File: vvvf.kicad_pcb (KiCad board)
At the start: 4 copper layers, 100 x 100 mm, 75 parts, among them Q3 IPDD60R037CM8XTMA1, Q4 IPDD60R037CM8XTMA1, Q5 IPDD60R037CM8XTMA1, Q6 IPDD60R037CM8XTMA1, Q7 IPDD60R037CM8XTMA1, Q8 IPDD60R037CM8XTMA1, Q9 IPDD60R037CM8XTMA1, U3 UCC21520ADW, U5 ACS770xCB-200B-PFF, U6 UCC21520ADW, U7 UCC21520ADW

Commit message: Continue on layout
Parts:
- C10, R11, R12, R14, R24, R25, R26, R27, R9: moved to B.Cu
- D12: moved to F.Cu
- moved R4 126.8 mm to (173.2, 76.8), turned to 90 degrees
- moved R9 115.4 mm to (180.2, 130.5), turned to -90 degrees
- moved C17 90.5 mm to (117.8, 76.8), turned to 90 degrees
- moved C18 90.2 mm to (113.5, 76.7), turned to 90 degrees
- moved C9 89.4 mm to (111.5, 76.8), turned to 90 degrees
- moved C19 79.3 mm to (112.9, 92.2), turned to 180 degrees
- moved R22 75.6 mm to (115.2, 76.7), turned to 90 degrees
- moved C22 71.5 mm to (119.2, 92.2), turned to 180 degrees
- moved C21 68.1 mm to (119.2, 94.8), turned to 180 degrees
- moved C20 65.0 mm to (119.2, 97.3), turned to 180 degrees
- moved R23 64.5 mm to (123.5, 100.2), turned to -90 degrees
- moved C23 61.3 mm to (239.0, 142.0)
- moved R24 60.8 mm to (123.5, 108.5), turned to -90 degrees
- moved R26 56.6 mm to (120.0, 115.8), turned to -90 degrees
- moved R25 50.9 mm to (123.5, 130.8), turned to -90 degrees
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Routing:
- net Net-(J2-Pin_1): track 0.00 -> 25.2 mm
- added copper zone on In2.Cu, net GND

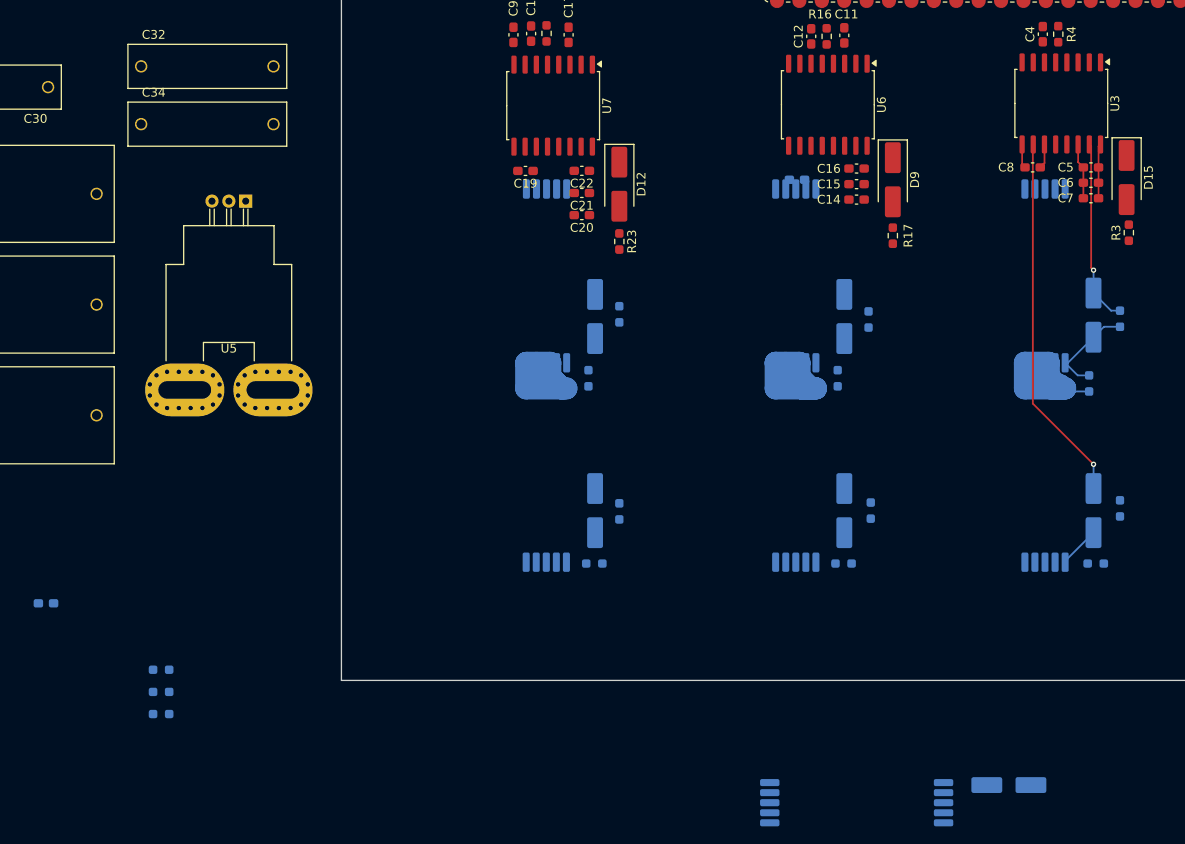
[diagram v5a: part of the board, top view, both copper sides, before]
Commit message: Checkpoint before switching to an external IGBT array
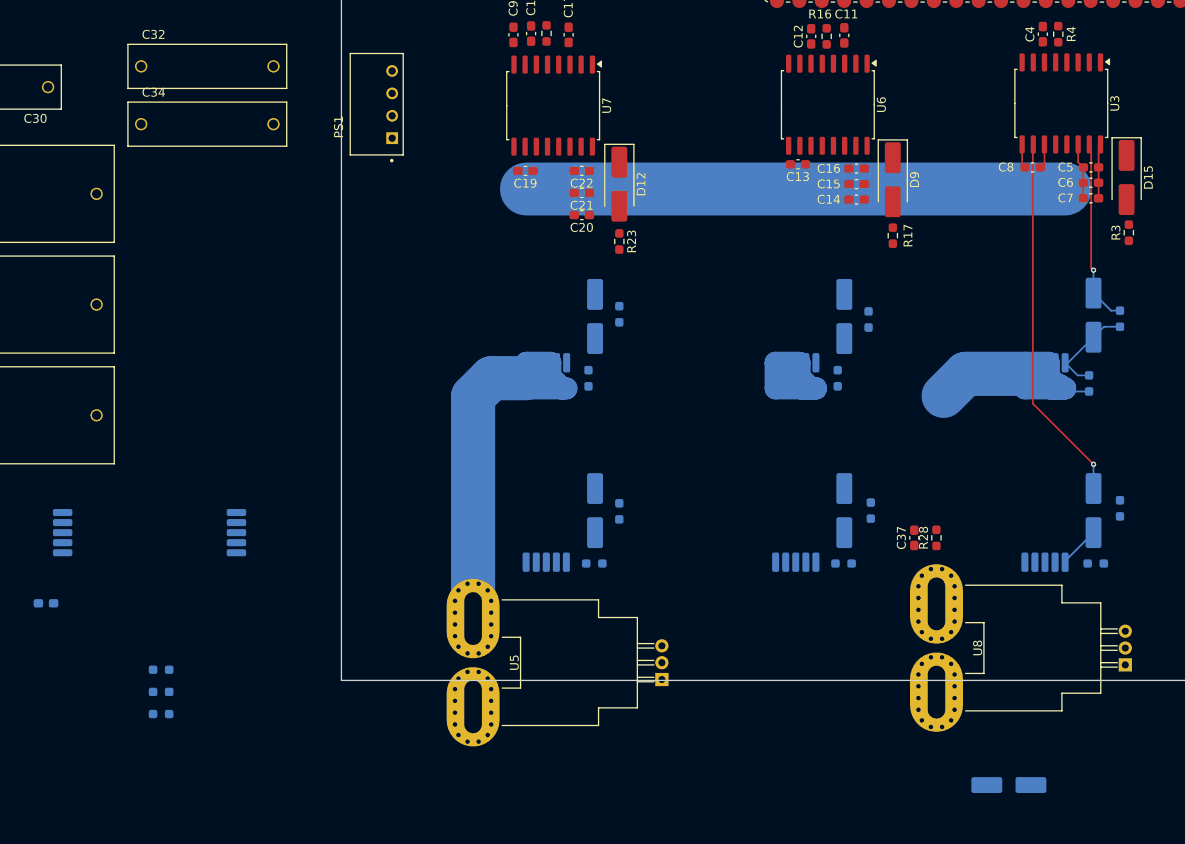
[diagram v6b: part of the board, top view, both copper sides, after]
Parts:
- added C37: 100nF, Capacitor_SMD:C_0603_1608Metric_Pad1.08x0.95mm_HandSolder, F.Cu at (156.9, 133.8)
- added PS1: ROE-1205S, Snapeda:ROE-1205S_CONV_ROE-1205S, F.Cu at (96.0, 84.7)
- added R28: 10k, Resistor_SMD:R_0603_1608Metric_Pad0.98x0.95mm_HandSolder, F.Cu at (159.4, 133.8)
- added U8: ACS770xCB-200B-PFF, Sensor_Current:Allegro_CB_PFF, F.Cu at (180.8, 148.2)
- C13: moved to F.Cu
- moved Q4 85.8 mm to (70.2, 133.2)
- moved U5 71.9 mm to (128.3, 149.9), turned to 90 degrees
- moved C13 1.75 mm to (143.8, 91.5)
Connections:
- net +24V renamed +12V
- A1 pad 36: unconnected-(A1-3V3-Pad36) -> +3V3
- C23 pad 2: Net-(J1-Pin_1) (its old number) -> /C3
- C24 pad 2: Net-(J1-Pin_1) (its old number) -> /C3
- C25 pad 1: Net-(J1-Pin_1) (its old number) -> /C3
- C26 pad 1: Net-(J1-Pin_1) (its old number) -> /C3
- C5 pad 2: Net-(J1-Pin_1) (its old number) -> /C3
- C6 pad 2: Net-(J1-Pin_1) (its old number) -> /C3
- C7 pad 2: Net-(J1-Pin_1) (its old number) -> /C3
- D7 pad 2: +3V3 -> +5V
- Q3 pad 10: Net-(J1-Pin_1) (its old number) -> /C3
- Q3 pad 6: Net-(J1-Pin_1) (its old number) -> /C3
- Q3 pad 7: Net-(J1-Pin_1) (its old number) -> /C3
- Q3 pad 8: Net-(J1-Pin_1) (its old number) -> /C3
- Q3 pad 9: Net-(J1-Pin_1) (its old number) -> /C3
- Q5 pad 2: Net-(J1-Pin_1) (its old number) -> /C3
- Q5 pad 3: Net-(J1-Pin_1) (its old number) -> /C3
- Q5 pad 4: Net-(J1-Pin_1) (its old number) -> /C3
- Q5 pad 5: Net-(J1-Pin_1) (its old number) -> /C3
- R5 pad 2: Net-(J1-Pin_1) (its old number) -> /C3
- U3 pad 14: Net-(J1-Pin_1) (its old number) -> /C3
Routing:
- net Vdrive: track 0.00 -> 61.1 mm
- net /C3: track 0.00 -> 45.2 mm
- net /C1: track 21.3 -> 56.2 mm
- net Net-(J1-Pin_1) (its old number): track 33.9 -> 0.00 mm

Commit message: Starting new routing with external IGBT
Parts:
- removed C10: 100nF, Capacitor_SMD:C_0603_1608Metric_Pad1.08x0.95mm_HandSolder
- removed C23, C25, C27, C29, C31, C33: 1uF, Snapeda:B32923C3105M000_CAPRR2250W80L2650T1100H2050
- removed C24, C26, C28, C30, C32, C34: 100nF, Snapeda:B32922C3104K289_CAPRR1500W80L1800T500H1050
- removed Q3, Q4, Q5, Q6, Q7, Q8, Q9: IPDD60R037CM8XTMA1, Package_TO_SOT_SMD:Infineon_PG-HDSOP-10-1
- removed R14: 10k, Resistor_SMD:R_0603_1608Metric_Pad0.98x0.95mm_HandSolder
- removed U5: ACS770xCB-200B-PFF, Sensor_Current:Allegro_CB_PFF
- added C38: 100nF, Capacitor_SMD:C_0603_1608Metric_Pad1.08x0.95mm_HandSolder, F.Cu at (65.6, 93.2)
- added J1: Conn_01x16_Pin, Connector_PinHeader_2.54mm:PinHeader_1x16_P2.54mm_Vertical, F.Cu at (150.9, 120.6)
- added J2: Screw_Terminal_01x01, easyeda2kicad:CONN-TH_T44001, F.Cu at (35.0, 134.3)
- added J3: Screw_Terminal_01x01, easyeda2kicad:CONN-TH_T44001, F.Cu at (44.3, 134.3)
- added J6: Screw_Terminal_01x02, easyeda2kicad:CONN-TH_WJ126V-5.0-2P, F.Cu at (97.5, 97.0)
- added J7: Screw_Terminal_01x01, easyeda2kicad:CONN-TH_T44001, F.Cu at (69.8, 130.5)
- added J8: Screw_Terminal_01x01, easyeda2kicad:CONN-TH_T44001, F.Cu at (59.8, 131.0)
- added R30: 10k, Resistor_SMD:R_0603_1608Metric_Pad0.98x0.95mm_HandSolder, F.Cu at (65.6, 95.8)
- added U4: TLP152, Package_SO:SO-5-6_4.55x3.7mm_P1.27mm, F.Cu at (61.8, 156.5)
- added U9: ACS758KCB-150B-PFF-T, easyeda2kicad:SENSOR-TH_ACS758KCB-150B-PFF-T, F.Cu at (40.0, 112.6)
- D10, D11, D13, D3, D5, D6, D8, R10, R11, R12, R18, R19, R20, R21, R24, R25, R26, R27, R5, R6, R9: moved to F.Cu
- U8: value ACS770xCB-200B-PFF -> ACS758KCB-150B-PFF-T; footprint Sensor_Current:Allegro_CB_PFF -> easyeda2kicad:SENSOR-TH_ACS758KCB-150B-PFF-T
- moved C37 124.0 mm to (40.0, 92.6)
- moved R28 124.0 mm to (42.5, 92.6)
- moved U8 122.8 mm to (64.2, 109.6), turned to 180 degrees
- moved D6 94.1 mm to (74.0, 153.0), turned to 0 degrees
- moved R25 37.1 mm to (144.3, 100.2)
- moved D13 36.9 mm to (141.5, 100.3)
- moved R27 33.4 mm to (141.3, 110.5), turned to -90 degrees
- moved D5 32.9 mm to (159.0, 99.4)
- moved R19 32.8 mm to (161.7, 99.4)
- moved R23 32.8 mm to (154.8, 90.7)
- moved D3 32.2 mm to (176.9, 98.5)
- moved R9 32.0 mm to (179.7, 98.5)
- moved R21 30.4 mm to (160.1, 108.5)
- moved R26 29.6 mm to (149.3, 111.4), turned to 90 degrees
- moved C18 29.3 mm to (142.8, 78.0)
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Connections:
- net /C1 renamed /IGBT_W_H_E
- net Net-(D10-A) renamed /IGBT_V_H_G
- net Net-(D11-A) renamed /IGBT_W_H_G
- net Net-(D13-A) renamed /IGBT_W_L_G
- net Net-(D3-A) renamed /IGBT_U_L_G
- net Net-(D5-A) renamed /IGBT_V_L_G
- net Net-(D6-A) renamed /IGBT_BRAKE_G
- net Net-(D8-A) renamed /IGBT_U_H_G
- net Net-(J1-Pin_1) renamed /IGBT_V_H_E
- C5 pad 2: /C3 -> /IGBT_U_H_E
- C6 pad 2: /C3 -> /IGBT_U_H_E
- C7 pad 2: /C3 -> /IGBT_U_H_E
- R28 pad 1: Net-(U8-VIOUT) -> Net-(U9-VOUT)
- R28 pad 2: /GP26 -> /ADC1
- R5 pad 2: /C3 -> /IGBT_U_H_E
- U3 pad 14: /C3 -> /IGBT_U_H_E
- U8 pad 3: Net-(U8-VIOUT) -> Net-(U8-VOUT)
- U8 pad 4: /C3 -> Net-(J8-Pin_1)
- U8 pad 5: /C4 -> Net-(J7-Pin_1)
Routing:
- net Vdrive: track 61.1 -> 0.00 mm
- net /IGBT_W_H_E: track 56.2 -> 6.49 mm
- net /C3: track 45.2 -> 0.00 mm
- net Net-(D3-K): track 41.9 -> 9.87 mm, vias 1 -> 0
- net /IGBT_V_H_E: track 25.2 -> 6.30 mm
- net GND: track 0.00 -> 16.5 mm, vias 0 -> 2
- net +5V: track 0.00 -> 15.7 mm
- net Net-(D11-K): track 0.00 -> 13.3 mm
- net Net-(D10-K): track 0.00 -> 13.1 mm
- net Net-(D13-K): track 0.00 -> 10.8 mm
- net Net-(D5-K): track 0.00 -> 10.3 mm
- net Net-(D9-K): track 0.00 -> 9.69 mm
- net Net-(D12-K): track 0.00 -> 9.63 mm
- net /IGBT_U_H_G: track 11.2 -> 3.41 mm
- net Net-(D8-K): track 20.9 -> 13.3 mm, vias 1 -> 0
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
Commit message: sus commit
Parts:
- added C10: 100nF, Capacitor_SMD:C_0603_1608Metric_Pad1.08x0.95mm_HandSolder, F.Cu at (43.4, 78.9)
- added J4: Screw_Terminal_01x01, easyeda2kicad:CONN-TH_T44001, F.Cu at (77.8, 74.7)
- added J5: Screw_Terminal_01x01, easyeda2kicad:CONN-TH_T44001, F.Cu at (77.8, 84.0)
- added J9: Screw_Terminal_01x02, easyeda2kicad:CONN-TH_WJ126V-5.0-2P, F.Cu at (97.6, 107.9)
- added R13: 10k, Resistor_SMD:R_0603_1608Metric_Pad0.98x0.95mm_HandSolder, F.Cu at (40.9, 78.9)
- added R14: 6.8k, Resistor_SMD:R_0603_1608Metric_Pad0.98x0.95mm_HandSolder, F.Cu at (44.3, 76.3)
- added R15: 1M, Resistor_SMD:R_1206_3216Metric_Pad1.30x1.75mm_HandSolder, F.Cu at (110.8, 102.4)
- added R29: 6.8k, Resistor_SMD:R_0603_1608Metric_Pad0.98x0.95mm_HandSolder, F.Cu at (50.3, 109.2)
- added R31: 6.8k, Resistor_SMD:R_0603_1608Metric_Pad0.98x0.95mm_HandSolder, F.Cu at (27.5, 109.4)
- added R32: 1k, Resistor_SMD:R_1206_3216Metric_Pad1.30x1.75mm_HandSolder, F.Cu at (120.8, 102.4)
- added R33: 1M, Resistor_SMD:R_1206_3216Metric_Pad1.30x1.75mm_HandSolder, F.Cu at (115.8, 102.4)
- added U11: LM7805_TO220, Package_TO_SOT_THT:TO-220-3_Vertical, F.Cu at (110.4, 96.0)
- added U12: AMC1303M2510DWVR, easyeda2kicad:SOIC-8_L7.5-W5.9-P1.27-LS11.5-BL-1, F.Cu at (121.8, 86.0)
- added U5: ACS758KCB-150B-PFF-T, easyeda2kicad:SENSOR-TH_ACS758KCB-150B-PFF-T, F.Cu at (58.8, 79.6)
- moved R12 121.5 mm to (182.0, 111.4), turned to 180 degrees
- moved R11 110.9 mm to (176.6, 124.2)
- moved D6 107.5 mm to (176.8, 121.4)
- moved U4 100.8 mm to (133.4, 85.6), turned to -90 degrees
- moved J7 43.2 mm to (27.9, 141.5)
- moved C38 43.2 mm to (24.4, 106.2)
- moved U8 43.2 mm to (23.0, 122.5)
- moved R30 43.2 mm to (24.4, 108.7)
- moved J8 43.1 mm to (17.9, 141.5)
- moved R27 38.4 mm to (179.2, 116.6), turned to 0 degrees
- moved J2 24.9 mm to (59.0, 140.6), turned to 180 degrees
- moved R5 23.0 mm to (161.5, 116.6), turned to 0 degrees
- moved C37 19.8 mm to (53.6, 107.0)
- moved R28 19.8 mm to (56.1, 107.0)
- moved U9 17.3 mm to (54.6, 121.9)
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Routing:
- net +5V: track 15.7 -> 155.0 mm, vias 0 -> 1
- net +12V: track 6.99 -> 141.5 mm, vias 0 -> 1
- net Net-(D6-K): track 0.00 -> 68.8 mm
- net /IGBT_W_L_G: track 3.44 -> 46.9 mm, vias 0 -> 1
- net /IGBT_U_H_E: track 6.35 -> 37.4 mm, vias 0 -> 1
- net /IGBT_U_H_G: track 3.41 -> 33.2 mm
- net GNDPWR: track 8.86 -> 37.5 mm, vias 2 -> 4
- net /IGBT_V_H_E: track 6.30 -> 33.3 mm
- net /IGBT_V_H_G: track 3.18 -> 27.2 mm, vias 0 -> 2
- net /IGBT_V_L_G: track 3.41 -> 27.4 mm, vias 0 -> 1
- net /IGBT_W_H_E: track 6.49 -> 30.0 mm
- net /IGBT_U_L_G: track 3.41 -> 23.1 mm, vias 0 -> 1
- net /IGBT_BRAKE_G: track 0.00 -> 15.2 mm
- net Net-(U12-AINP): track 0.00 -> 13.7 mm
- net Vdrive: track 0.00 -> 12.8 mm
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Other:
- board text added: "12V"
- board text added: "GNDPWR"
- board text added: "Vdrive (HV)"
